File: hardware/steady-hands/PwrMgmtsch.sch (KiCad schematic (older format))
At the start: 27 parts

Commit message: Edits power management components
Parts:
- added TP?: +1V3, symbol Connector:TestPoint
- added TP?: +3V3, symbol Connector:TestPoint
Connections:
- wire segments 108 -> 110
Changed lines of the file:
@@
 Connection ~ 8050 3200
 $Comp
-L steady-hands-rescue:+1V3-steady-hands-cache #PWR?
+L steady-hands:+1V3 #PWR?
 U 1 1 5F0C6788
 P 9900 2600
@@
 	1    0    0    -1
 $EndComp
-Wire Wire Line
-	9900 2550 10050 2550
-Connection ~ 9900 2550
-Text HLabel 10050 2550 2    50   Output ~ 0
+Text HLabel 10250 2550 2    50   Output ~ 0
 +1V3
 Wire Wire Line
-	10350 4400 10550 4400
+	10350 4400 10400 4400
 Connection ~ 10350 4400
 Text HLabel 10550 4400 2    50   Output ~ 0
@@
 	7750 2550 8300 2550
 Connection ~ 7750 2550
+$Comp
+L Connector:TestPoint TP?
+U 1 1 5F0707ED
+P 10000 2550
+F 0 "TP?" H 9950 2600 50  0000 R CNN
+F 1 "+1V3" H 9950 2700 50  0000 R CNN
+F 2 "" H 10200 2550 50  0001 C CNN
+F 3 "~" H 10200 2550 50  0001 C CNN
+	1    10000 2550
+	-1   0    0    1
+$EndComp
+Wire Wire Line
+	9900 2550 10000 2550
+Connection ~ 9900 2550
+Connection ~ 10000 2550
+Wire Wire Line
+	10000 2550 10250 2550
+$Comp
+L Connector:TestPoint TP?
+U 1 1 5F07BA93
+P 10400 4400
+F 0 "TP?" H 10350 4450 50  0000 R CNN
+F 1 "+3V3" H 10350 4550 50  0000 R CNN
+F 2 "" H 10600 4400 50  0001 C CNN
+F 3 "~" H 10600 4400 50  0001 C CNN
+	1    10400 4400
+	-1   0    0    1
+$EndComp
+Connection ~ 10400 4400
+Wire Wire Line
+	10400 4400 10550 4400
 $EndSCHEMATC

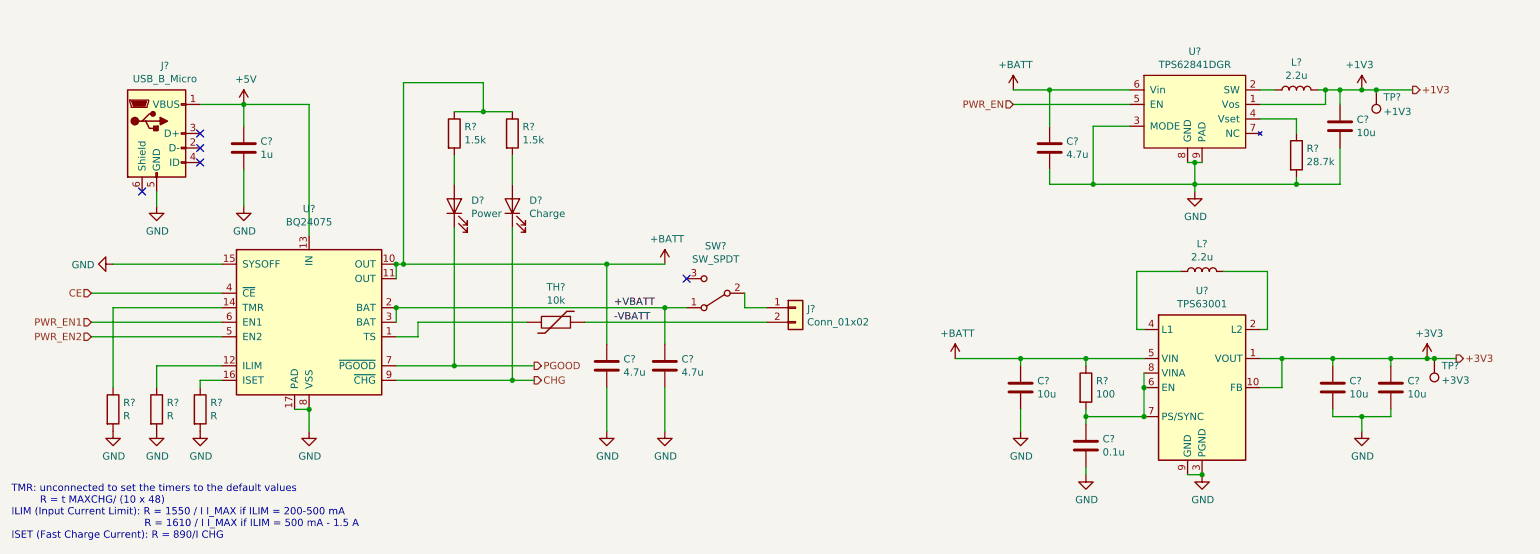
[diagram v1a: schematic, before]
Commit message: Completes schematic connections
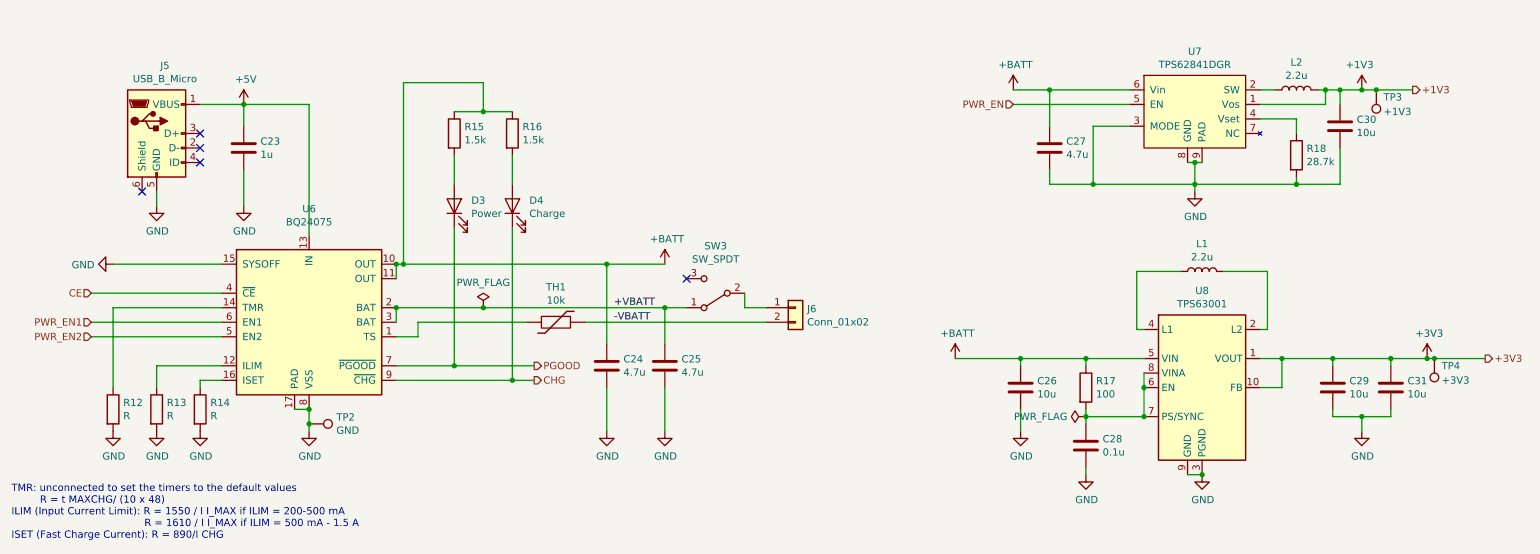
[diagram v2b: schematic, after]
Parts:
- added TP2: GND, TestPoint:TestPoint_Pad_1.0x1.0mm, symbol Connector:TestPoint
- gave numbers to parts that had none: 29
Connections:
- net GND: now also TP2.1
